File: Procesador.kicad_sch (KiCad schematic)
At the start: 0 parts

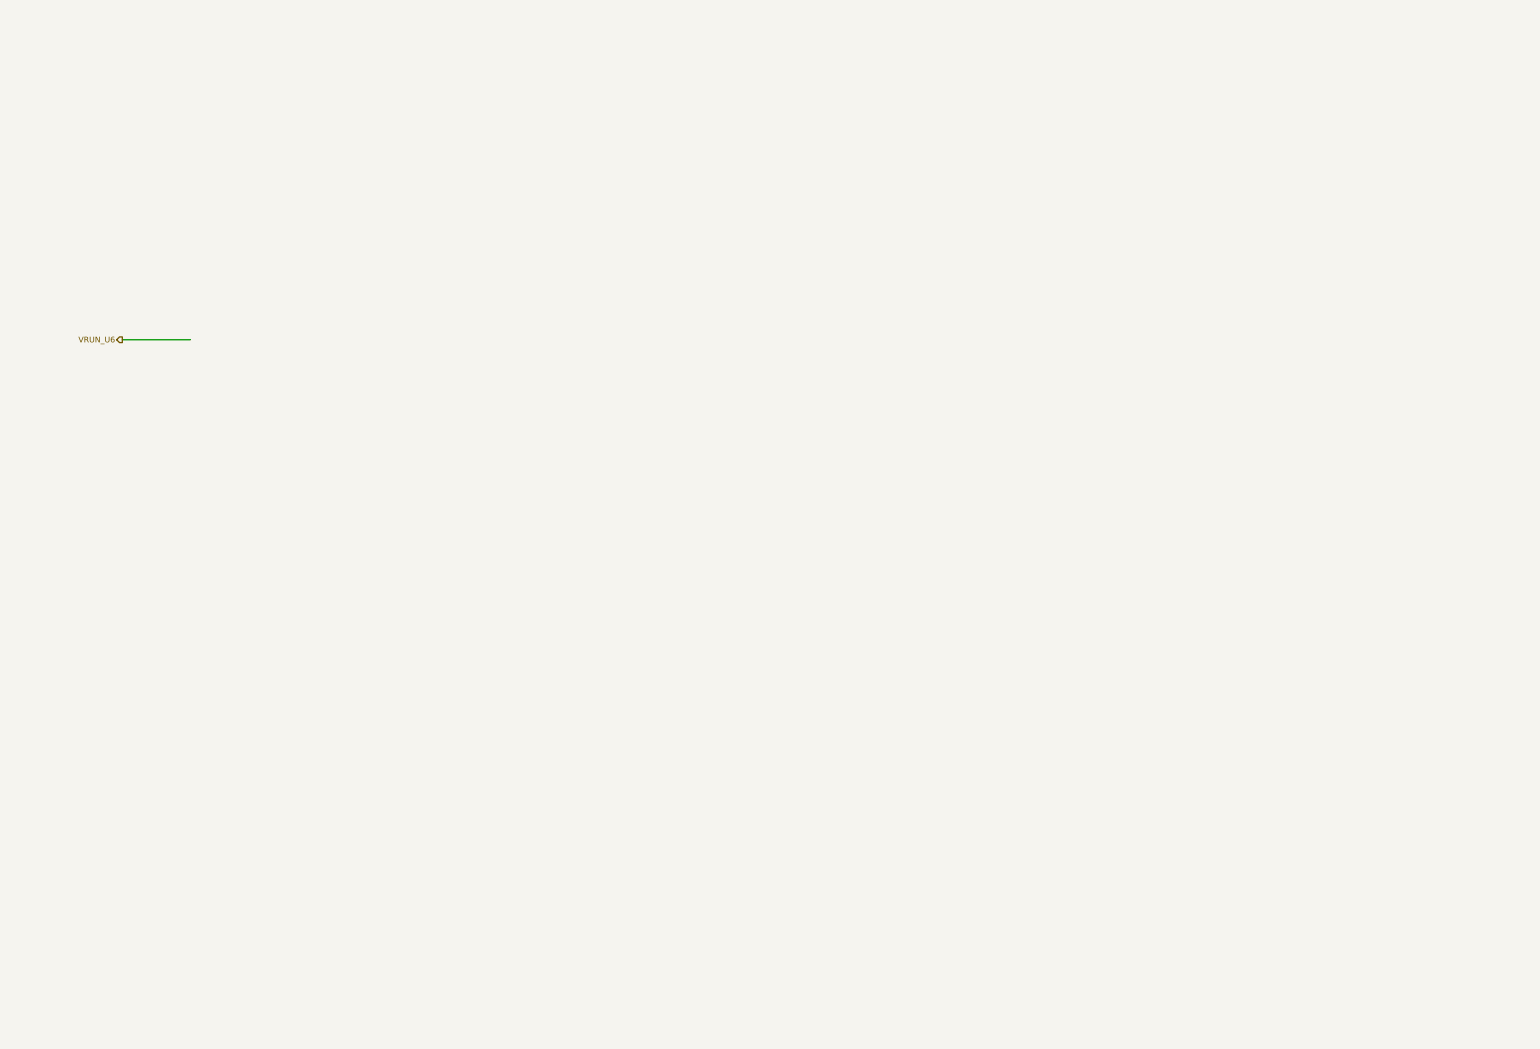
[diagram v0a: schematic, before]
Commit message: 13-Mayo26 se agrego hoja de procesador y USB
hoja de USB AL 95% HOJA DEL procesador al 75%
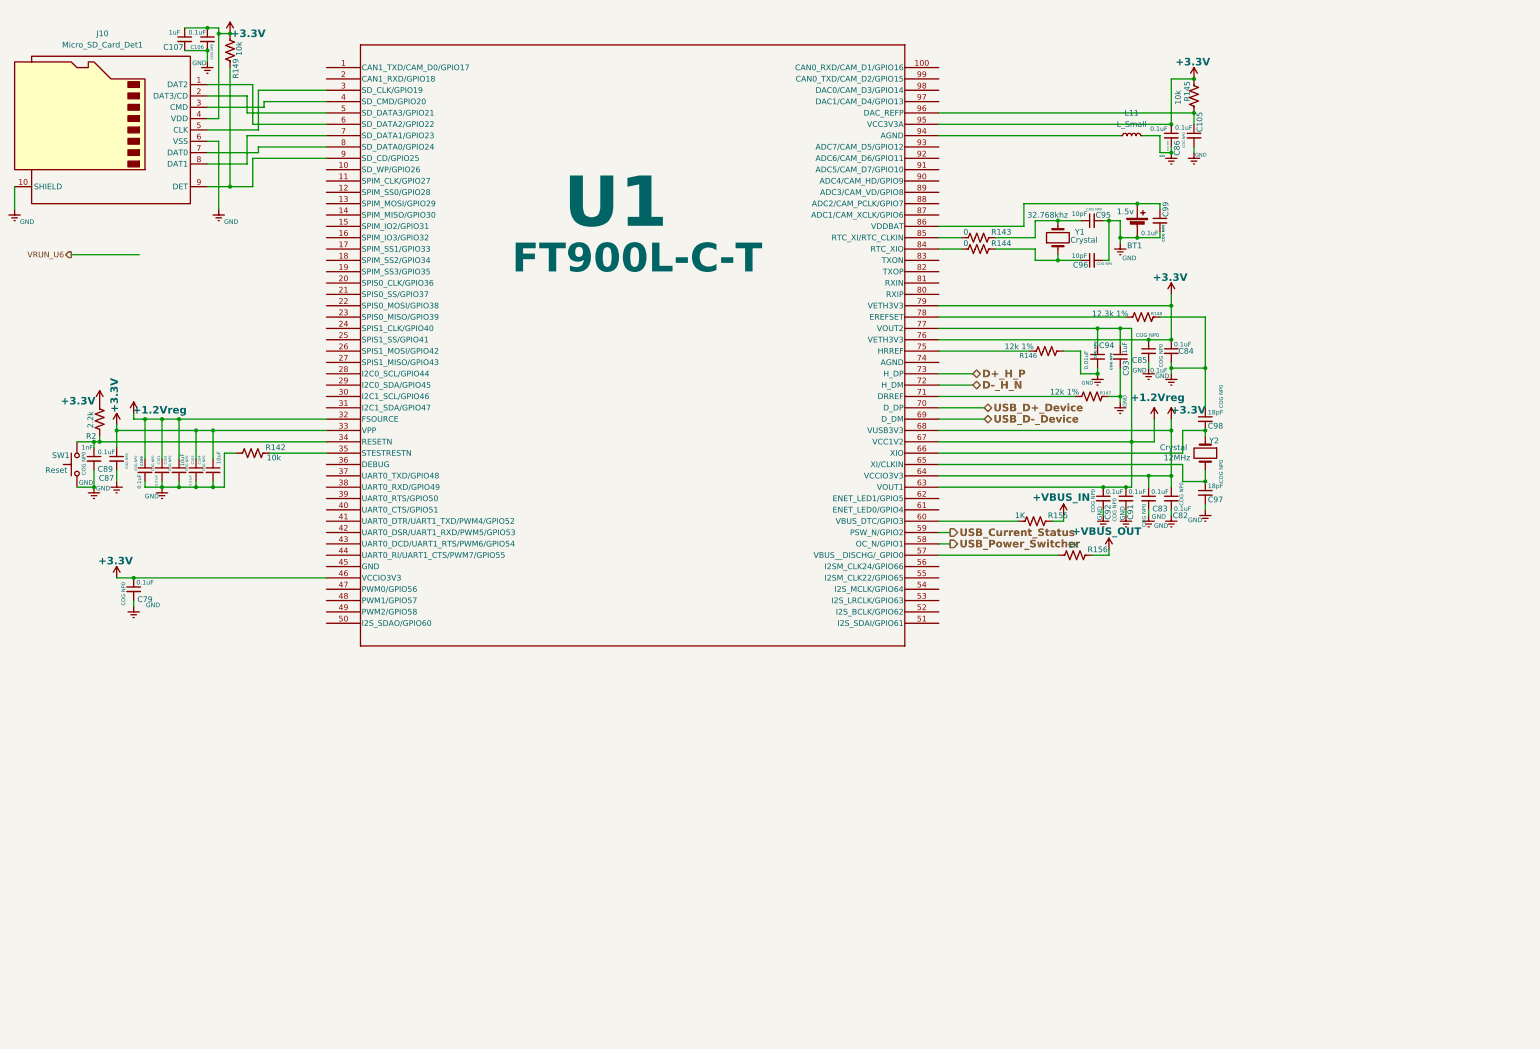
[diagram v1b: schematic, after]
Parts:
- added BT1: 1.5v, symbol Device:Battery_Cell
- added C100, C105, C106, C79, C82, C83, C84, C85, C86, C87, C91, C92, C99: 0.1uF, Capacitor_SMD:C_0603_1608Metric_Pad1.08x0.95mm_HandSolder, symbol Device:C_Small
- added C101, C103, C94: 0.01uF, Capacitor_SMD:C_0603_1608Metric_Pad1.08x0.95mm_HandSolder, symbol Device:C_Small
- added C102, C104: 10uF, symbol Device:C_Small
- added C107: 1uF, symbol Device:C_Small
- added C89: 1nF, Capacitor_SMD:C_0603_1608Metric_Pad1.08x0.95mm_HandSolder, symbol Device:C_Small
- added C93: 1uF, Capacitor_SMD:C_0603_1608Metric_Pad1.08x0.95mm_HandSolder, symbol Device:C_Small
- added C95, C96: 10pF, Capacitor_SMD:C_0603_1608Metric_Pad1.08x0.95mm_HandSolder, symbol Device:C_Small
- added C97, C98: 18pF, Capacitor_SMD:C_0603_1608Metric_Pad1.08x0.95mm_HandSolder, symbol Device:C_Small
- added J10: Micro_SD_Card_Det1, symbol Connector:Micro_SD_Card_Det1
- added L11: L_Small, symbol Device:L_Small
- added R142, R145, R149: 10k, Resistor_SMD:R_0603_1608Metric, symbol Device:R_US
- added R143, R144: 0, Resistor_SMD:R_0603_1608Metric, symbol Device:R_US
- added R146, R147: 12k 1%, Resistor_SMD:R_0603_1608Metric, symbol Device:R_US
- added R148: 12.3k 1%, Resistor_SMD:R_0603_1608Metric, symbol Device:R_US
- added R155, R156: 1K, Resistor_SMD:R_0603_1608Metric, symbol Device:R_US
- added R2: 2.2k, Resistor_SMD:R_0603_1608Metric, symbol Device:R_US
- added SW1: Reset, symbol Switch:SW_Push
- added U1: FT900L-C-T, footprints:LQFP_100_14X14X1P4_BRI, symbol MICROS_DIGITAL_GSI:FT900L-C-T
- added Y1, Y2: Crystal, symbol Device:Crystal
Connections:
- new net: C97.1, U1.65 (XI/CLKIN), Y2.2
- new net: C89.1, R2.1, SW1.2, U1.34 (RESETN)
- new net: C95.1, R143.1, Y1.2
- new net: C96.1, R144.1, Y1.1
- new net: BT1.1 (+), C99.1, U1.86 (VDDBAT)
- new net: C98.2, U1.66 (XIO), Y2.1
- new net: R148.1, U1.78 (EREFSET)
- new net: J10.9 (DET), R149.2, U1.9 (SD_CD/GPIO25)
- new net: L11.1, U1.94 (AGND)
- new net: R155.2, U1.60 (VBUS_DTC/GPIO3)
- new net: C105.1, R145.2, U1.96 (DAC_REFP)
- new net: R146.1, U1.75 (HRREF)
- new net: J10.5 (CLK), U1.3 (SD_CLK/GPIO19)
- new net: R142.1, U1.35 (STESTRESTN)
- new net: J10.3 (CMD), U1.4 (SD_CMD/GPIO20)
- new net: J10.2 (DAT3/CD), U1.5 (SD_DATA3/GPIO21)
- new net: R156.2, U1.57 (VBUS__DISCHG/_GPIO0)
- new net: J10.1 (DAT2), U1.6 (SD_DATA2/GPIO22)
- new net: J10.8 (DAT1), U1.7 (SD_DATA1/GPIO23)
- new net: R147.1, U1.71 (DRREF)
- new net: J10.7 (DAT0), U1.8 (SD_DATA0/GPIO24)
- new net: R144.2, U1.84 (RTC_XIO)
- new net: R143.2, U1.85 (RTC_XI/RTC_CLKIN)
- new net +1.2Vreg: C100.1, C101.1, C102.1, C91.1, C92.1, C93.1, C94.1, U1.32 (FSOURCE), U1.63 (VOUT1), U1.67 (VCC1V2), U1.77 (VOUT2)
- new net +3.3V: C103.1, C104.1, C106.1, C107.1, C79.1, C82.1, C83.1, C84.1, C85.1, C86.1, C87.1, J10.4 (VDD), R145.1, R149.1, R2.2, U1.33 (VPP), U1.46 (VCCIO3V3), U1.64 (VCCIO3V3), U1.68 (VUSB3V3), U1.76 (VETH3V3), U1.79 (VETH3V3), U1.95 (VCC3V3A)
- new net +VBUS_IN: R155.1
- new net +VBUS_OUT: R156.1
- new net D+_H_P: U1.73 (H_DP)
- new net D-_H_N: U1.72 (H_DM)
- new net GND: BT1.2 (-), C100.2, C101.2, C102.2, C103.2, C104.2, C105.2, C106.2, C107.2, C79.2, C82.2, C83.2, C84.2, C85.2, C86.2, C87.2, C89.2, C91.2, C92.2, C93.2, C94.2, C95.2, C96.2, C97.2, C98.1, C99.2, J10.10 (SHIELD), J10.6 (VSS), L11.2, R142.2, R146.2, R147.2, R148.2, SW1.1
- new net USB_Current_Status: U1.59 (PSW_N/GPIO2)
- new net USB_D+_Device: U1.70 (D_DP)
- new net USB_D-_Device: U1.69 (D_DM)
- new net USB_Power_Switcher: U1.58 (OC_N/GPIO1)

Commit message: 14-Mayo-26
se agregaron varias sheet de esquematico crecio al 80% la parte de esquematico
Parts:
- removed L11: L_Small, symbol Device:L_Small
- added C116, C117, C118, C119, C85: 0.1uF, Capacitor_SMD:C_0603_1608Metric_Pad1.08x0.95mm_HandSolder, symbol Device:C_Small
- added CN7: 10way 1.27mm, CONECTORES GRACIDA:MicroMatch_10way_P1.75mm, symbol CONECTORES GRACIDA:1-215079-0_microMatch10P_1.27mm
- added D32: PMEG2010BER, Diode_SMD:Nexperia_CFP3_SOD-123W, symbol Diode:PMEG2010BER
- added J15: RJ45_Wuerth_7499010211A, Connector_RJ:RJ45_Wuerth_7499010211A_Horizontal, symbol Connector:RJ45_Wuerth_7499010211A
- added L14, L15: L_Iron_Small, symbol Device:L_Iron_Small
- added R160, R161: 1K, Resistor_SMD:R_0603_1608Metric, symbol Device:R_US
- added R162, R163: 160, Resistor_SMD:R_0603_1608Metric, symbol Device:R_US
- added R164, R165, R166, R167: 49.9R, Resistor_SMD:R_0603_1608Metric, symbol Device:R_US
- added U6: 24AA02E-OT, Package_TO_SOT_SMD:SOT-23-5, symbol Memory_EEPROM:24AA02E-OT
- renumbered C85 to C100, C83 to C101, C99 to C102, C86 to C103, C84 to C104, C82 to C105, C105 to C106, C98 to C107, C97 to C108, C89 to C83, C87 to C84, C79 to C86, C100 to C87, C101 to C88, C102 to C89, C107 to C90, C103 to C91, C106 to C92, C104 to C93, C95 to C94, C96 to C95, C94 to C96, C92 to C97, C93 to C98, C91 to C99, J10 to J11, R2 to R141, R149 to R142, R142 to R143, R143 to R144, R144 to R145, R155 to R146, R146 to R147, R156 to R148, R147 to R149, R148 to R150, R145 to R151
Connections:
- net +3.3V: now also C116.1, C117.1, J15.4 (CTD), J15.5 (CRD), R160.2, R161.2, R162.2, R163.2, U6.4 (V_{CC})
- net GND: now also U1.45 (GND), C116.2, C117.2, C118.2, C119.1, C85.2, CN7. (9), J15.8, J15.SH, L14.1, L15.1, U6.2 (V_{SS})
- net USB_Current_Status: now also U1.58 (OC_N/GPIO1); no longer U1.59 (PSW_N/GPIO2)
- net USB_Power_Switcher: now also U1.59 (PSW_N/GPIO2); no longer U1.58 (OC_N/GPIO1)
- net at C83.1, R141.1, SW1.2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: now also CN7. (9)
- net at U1.94 (AGND): now also L15.2
- net at U1.20 (SPIS0_CLK/GPIO36): now also CN7. (9)
- net at U1.21 (SPIS0_SS/GPIO37): now also CN7. (9)
- net at U1.22 (SPIS0_MOSI/GPIO38): now also CN7. (9)
- net at U1.23 (SPIS0_MISO/GPIO39): now also CN7. (9)
- net at U1.30 (I2C1_SCL/GPIO46): now also R160.1, U6.1 (SCL)
- net at U1.31 (I2C1_SDA/GPIO47): now also R161.1, U6.3 (SDA)
- net at U1.36 (DEBUG): now also CN7. (9)
- net at U1.61 (ENET_LED0/GPIO4): now also J15.11
- net at U1.62 (ENET_LED1/GPIO5): now also J15.10
- net at U1.74 (AGND): now also L14.2
- net at U1.80 (RXIP): now also J15.3 (RD+), R165.2
- net at U1.81 (RXIN): now also J15.6 (RD-), R164.2
- net at U1.82 (TXOP): now also J15.1 (TD+), R167.2
- net at U1.83 (TXON): now also J15.2 (TD-), R166.2
- new net: C119.2, R166.1, R167.1
- new net: J15.9, R163.1
- new net: J15.12, R162.1
- new net: C118.1, R164.1, R165.1
- new net +5V: D32.1 (K)
- new net DBG_5V: C85.1, CN7. (9), D32.2 (A)
- no-connect marks 0 -> 2
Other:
- note added: "act led"
- note added: "speed Led"
- note added: "verde"
- moved on the sheet: BT1, C102, C103, C106, C94, C95, R144, R145, R146, R148, R151, Y1

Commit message: 15-mayo-26
15 mayo 26
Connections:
- net SPIM_SCLK: now reaches U1.11 (SPIM_CLK/GPIO27)
- net SPIM_MOSI: now reaches U1.13 (SPIM_MOSI/GPIO29)
- net SPIM_MISO: now reaches U1.14 (SPIM_MISO/GPIO30)
- net SPIM_SS: now reaches U1.19 (SPIM_SS3/GPIO35)
- net UART0_TXD: now reaches U1.37 (UART0_TXD/GPIO48)
- net UART0_RXD: now reaches U1.38 (UART0_RXD/GPIO49)
- net UART1_TXD: now reaches U1.41 (UART0_DTR/UART1_TXD/PWM4/GPIO52)
- net UART1_RXD: now reaches U1.42 (UART0_DSR/UART1_RXD/PWM5/GPIO53)
- net PD_N: now reaches U1.49 (PWM2/GPIO58)
- no-connect marks 2 -> 3
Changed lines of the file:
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@@
 	)
 	(no_connect
+		(at 106.68 45.72)
+	)
+	(no_connect
 		(at 30.48 82.55)
 	)
@@
 	(wire
 		(pts
+			(xy 104.14 53.34) (xy 106.68 53.34)
+		)
+		(stroke
+			(width 0)
+			(type default)
+		)
+	)
+	(wire
+		(pts
 			(xy 218.44 124.46) (xy 218.44 123.19)
 		)
@@
 	(wire
 		(pts
+			(xy 91.44 127) (xy 106.68 127)
+		)
+		(stroke
+			(width 0)
+			(type default)
+		)
+	)
+	(wire
+		(pts
 			(xy 207.01 63.5) (xy 215.9 63.5)
 		)
@@
 	(wire
 		(pts
+			(xy 104.14 68.58) (xy 106.68 68.58)
+		)
+		(stroke
+			(width 0)
+			(type default)
+		)
+	)
+	(wire
+		(pts
 			(xy 267.97 114.3) (xy 267.97 116.84)
 		)
@@
 	(wire
 		(pts
+			(xy 102.87 144.78) (xy 106.68 144.78)
+		)
+		(stroke
+			(width 0)
+			(type default)
+		)
+	)
+	(wire
+		(pts
 			(xy 69.85 30.48) (xy 106.68 30.48)
 		)
@@
 	(wire
 		(pts
-			(xy 106.68 134.62) (xy 104.14 134.62)
+			(xy 106.68 134.62) (xy 95.25 134.62)
 		)
 		(stroke
@@
 	(wire
 		(pts
+			(xy 91.44 116.84) (xy 106.68 116.84)
+		)
+		(stroke
+			(width 0)
+			(type default)
+		)
+	)
+	(wire
+		(pts
 			(xy 238.76 53.34) (xy 213.36 53.34)
 		)
@@
 	(wire
 		(pts
-			(xy 104.14 134.62) (xy 104.14 152.4)
+			(xy 95.25 134.62) (xy 95.25 152.4)
 		)
 		(stroke
@@
 	(wire
 		(pts
+			(xy 104.14 48.26) (xy 106.68 48.26)
+		)
+		(stroke
+			(width 0)
+			(type default)
+		)
+	)
+	(wire
+		(pts
 			(xy 67.31 49.53) (xy 67.31 43.18)
 		)
@@
 	(wire
 		(pts
+			(xy 91.44 124.46) (xy 106.68 124.46)
+		)
+		(stroke
+			(width 0)
+			(type default)
+		)
+	)
+	(wire
+		(pts
 			(xy 71.12 109.22) (xy 106.68 109.22)
 		)
@@
 	(wire
 		(pts
+			(xy 104.14 55.88) (xy 106.68 55.88)
+		)
+		(stroke
+			(width 0)
+			(type default)
+		)
+	)
+	(wire
+		(pts
 			(xy 106.68 76.2) (xy 57.15 76.2)
 		)
@@
 	(wire
 		(pts
+			(xy 91.44 114.3) (xy 106.68 114.3)
+		)
+		(stroke
+			(width 0)
+			(type default)
+		)
+	)
+	(wire
+		(pts
 			(xy 267.97 41.91) (xy 270.51 41.91)
 		)
@@
 		)
 	)
+	(hierarchical_label "PD_N"
+		(shape output)
+		(at 102.87 144.78 180)
+		(effects
+			(font
+				(size 1.27 1.27)
+				(thickness 0.254)
+				(bold yes)
+			)
+			(justify right)
+		)
+	)
+	(hierarchical_label "UART0_TXD"
+		(shape output)
+		(at 91.44 114.3 180)
+		(effects
+			(font
+				(size 1.27 1.27)
+				(thickness 0.254)
+				(bold yes)
+			)
+			(justify right)
+		)
+	)
 	(hierarchical_label "USB_D-_Device"
 		(shape bidirectional)
@@
 		)
 	)
+	(hierarchical_label "SPIM_SS"
+		(shape output)
+		(at 104.14 68.58 180)
+		(effects
+			(font
+				(size 1.27 1.27)
+				(thickness 0.254)
+				(bold yes)
+			)
+			(justify right)
+		)
+	)
 	(hierarchical_label "VRUN_U6"
 		(shape output)
@@
 		)
 	)
+	(hierarchical_label "SPIM_MISO"
+		(shape input)
+		(at 104.14 55.88 180)
+		(effects
+			(font
+				(size 1.27 1.27)
+				(thickness 0.254)
+				(bold yes)
+			)
+			(justify right)
+		)
+	)
+	(hierarchical_label "SPIM_MOSI"
+		(shape output)
+		(at 104.14 53.34 180)
+		(effects
+			(font
+				(size 1.27 1.27)
+				(thickness 0.254)
+				(bold yes)
+			)
+			(justify right)
+		)
+	)
 	(hierarchical_label "D+_H_P"
 		(shape bidirectional)
@@
 		)
 	)
+	(hierarchical_label "SPIM_SCLK"
+		(shape output)
+		(at 104.14 48.26 180)
+		(effects
+			(font
+				(size 1.27 1.27)
+				(thickness 0.254)
+				(bold yes)
+			)
+			(justify right)
+		)
+	)
+	(hierarchical_label "UART0_RXD"
+		(shape input)
+		(at 91.44 116.84 180)
+		(effects
+			(font
+				(size 1.27 1.27)
+				(thickness 0.254)
+				(bold yes)
+			)
+			(justify right)
+		)
+	)
+	(hierarchical_label "UART1_TXD"
+		(shape output)
+		(at 91.44 124.46 180)
+		(effects
+			(font
+				(size 1.27 1.27)
+				(thickness 0.254)
+				(bold yes)
+			)
+			(justify right)
+		)
+	)
+	(hierarchical_label "UART1_RXD"
+		(shape input)
+		(at 91.44 127 180)
+		(effects
+			(font
+				(size 1.27 1.27)
+				(thickness 0.254)
+				(bold yes)
+			)
+			(justify right)
+		)
+	)
 	(hierarchical_label "D-_H_N"
 		(shape bidirectional)
@@
 	(symbol
 		(lib_id "power:GNDREF")
-		(at 104.14 152.4 0)
+		(at 95.25 152.4 0)
 		(unit 1)
 		(exclude_from_sim no)
@@
 		(dnp no)
 		(property "Reference" "#PWR0281"
-			(at 104.14 158.75 0)
+			(at 95.25 158.75 0)
 			(effects
 				(font
@@
 		)
 		(property "Value" "GND"
-			(at 108.458 152.146 0)
+			(at 97.79 154.94 0)
 			(effects
 				(font
@@
 		)
 		(property "Footprint" ""
-			(at 104.14 152.4 0)
+			(at 95.25 152.4 0)
 			(effects
 				(font
@@
 		)
 		(property "Datasheet" ""
-			(at 104.14 152.4 0)
+			(at 95.25 152.4 0)
 			(effects
 				(font
@@
 		)
 		(property "Description" "Power symbol creates a global label with name \"GNDREF\" , reference supply ground"
-			(at 104.14 152.4 0)
+			(at 95.25 152.4 0)
 			(effects
 				(font

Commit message: 15-may-26
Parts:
- added U31: MCP9700Ax-ETT, Package_TO_SOT_SMD:SOT-23, symbol Sensor_Temperature:MCP9700Ax-ETT
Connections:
- net +3.3V: now also U31.1 (V_{DD})
- net GND: now also U31.3 (GND)
- net MO2: now reaches U1.1 (CAN1_TXD/CAM_D0/GPIO17)
- net Metal2: now reaches U1.100 (CAN0_RXD/CAM_D1/GPIO16)
- net !CS_Exp: now reaches U1.17 (SPIM_SS1/GPIO33)
- net !CS_J5_J6: now reaches U1.18 (SPIM_SS2/GPIO34)
- net MO3: now reaches U1.2 (CAN1_RXD/GPIO18)
- net INT_FT812: now reaches U1.40 (UART0_CTS/GPIO51)
- net METAL_INTERRUPCION: now reaches U1.43 (UART0_DCD/UART1_RTS/PWM6/GPIO54)
- net BUSY_DISPLAY: now reaches U1.44 (UART0_RI/UART1_CTS/PWM7/GPIO55)
- net MO1: now reaches U1.47 (PWM0/GPIO56)
- net INTA_J5_J6: now reaches U1.48 (PWM1/GPIO57)
- net at U1.87 (ADC1/CAM_XCLK/GPIO6): now also U31.2 (V_{OUT})
- net ADC2: now reaches U1.88 (ADC2/CAM_PCLK/GPIO7)
- net ADC3: now reaches U1.89 (ADC3/CAM_VD/GPIO8)
- net MO4: now reaches U1.93 (ADC7/CAM_D5/GPIO12)
- net DAC1: now reaches U1.97 (DAC1/CAM_D4/GPIO13)
- net DAC0: now reaches U1.98 (DAC0/CAM_D3/GPIO14)
- net Metal1: now reaches U1.99 (CAN0_TXD/CAM_D2/GPIO15)

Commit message: pcb 18 may 26
 falta poner la fuente de +12/ ya esta casi todo
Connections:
- net +3.3V: no longer C100.1, C101.1, C103.1, C104.1, C105.1, C84.1, C86.1, C90.1, C91.1, C92.1, C93.1, J11.4 (VDD), R142.1, R151.1, U1.33 (VPP), U1.46 (VCCIO3V3), U1.64 (VCCIO3V3), U1.68 (VUSB3V3), U1.76 (VETH3V3), U1.79 (VETH3V3), U1.95 (VCC3V3A)
- new net +3.3v_Fuse: C100.1, C101.1, C103.1, C104.1, C105.1, C84.1, C86.1, C90.1, C91.1, C92.1, C93.1, J11.4 (VDD), R142.1, R151.1, U1.33 (VPP), U1.46 (VCCIO3V3), U1.64 (VCCIO3V3), U1.68 (VUSB3V3), U1.76 (VETH3V3), U1.79 (VETH3V3), U1.95 (VCC3V3A)
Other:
- moved on the sheet: C86
